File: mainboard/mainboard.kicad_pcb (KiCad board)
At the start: 2 copper layers, 88.9 x 94 mm, 77 parts, among them U1 74HC04, U2 AS6C4008, U3 74HC32, U4 74HC00, U5 SST39SF040, U6 NE555, U7 74HCT245, U8 74HC574, U9 74HC574, Y1 Crystal

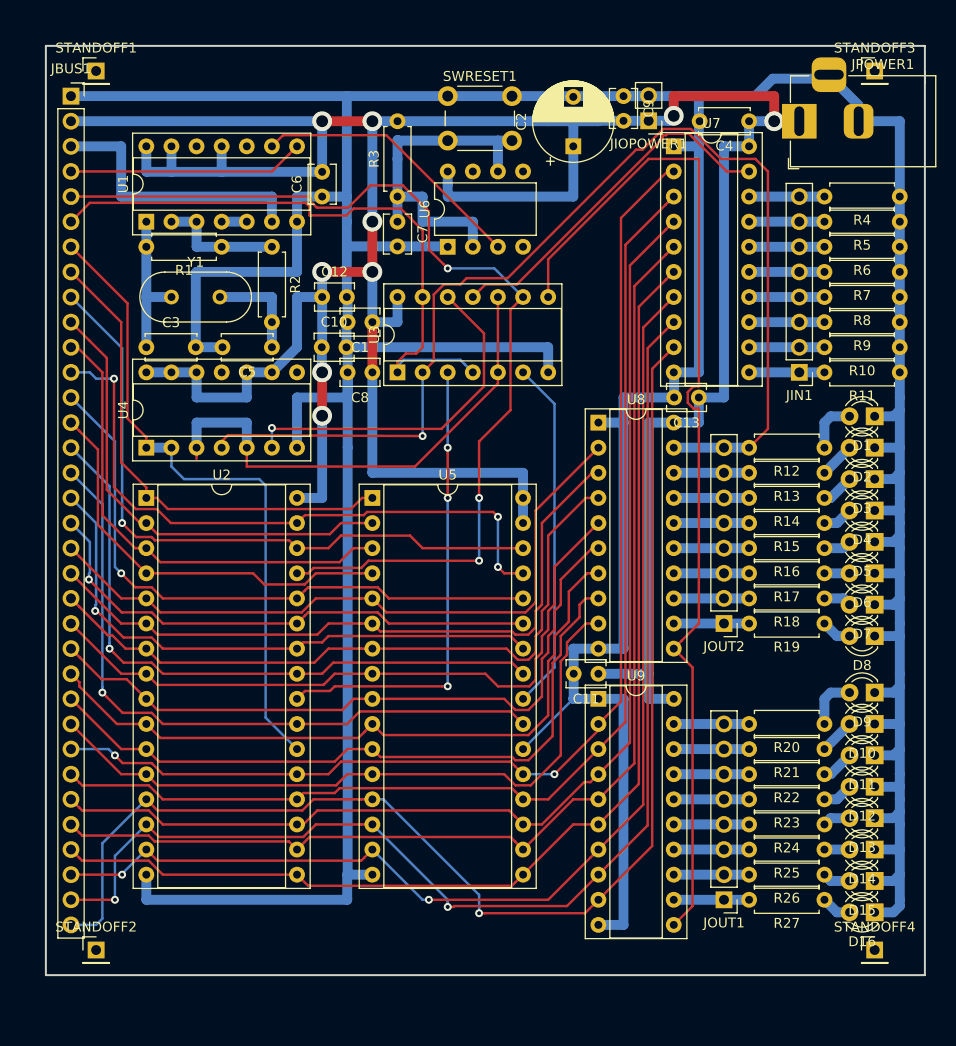
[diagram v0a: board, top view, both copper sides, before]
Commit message: Main board layout tweaks
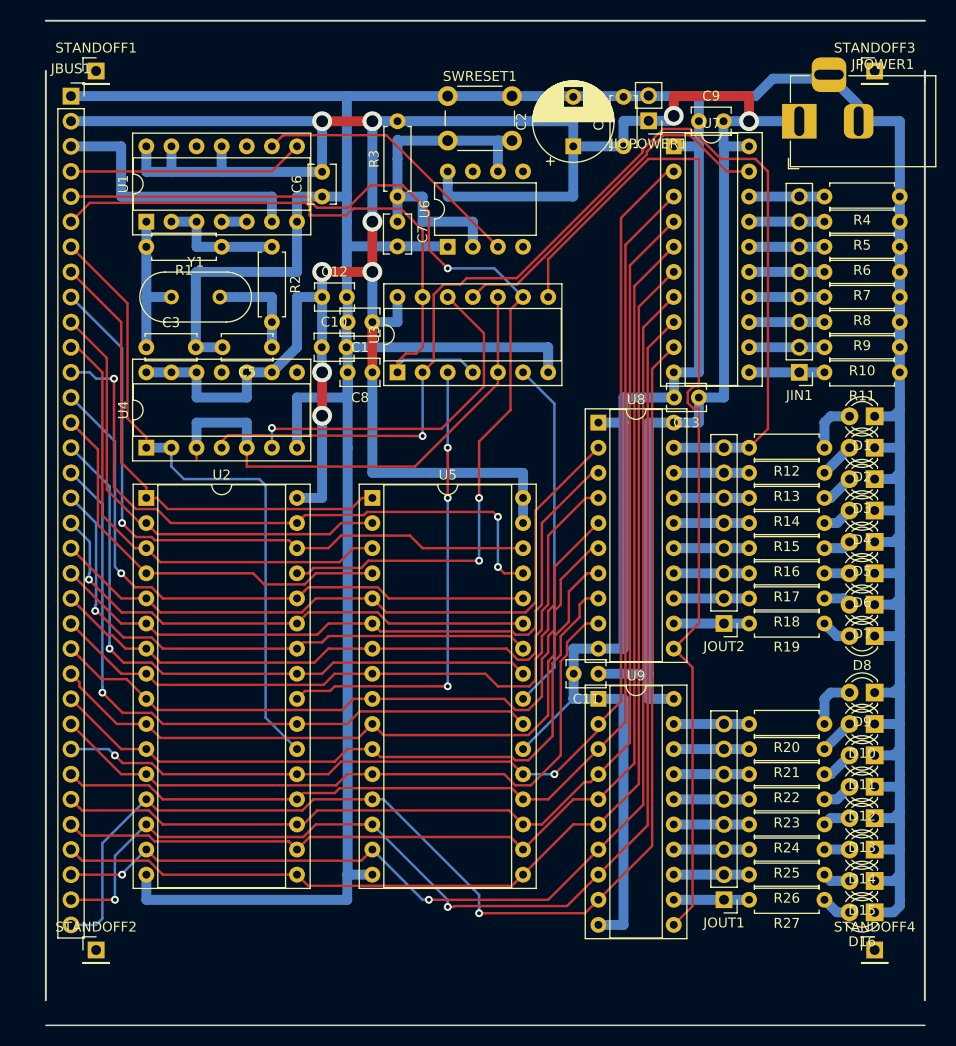
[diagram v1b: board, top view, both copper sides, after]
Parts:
- C3, C5: value 22pF -> 47pF
- moved C4 13.0 mm to (124.5, 50.8), turned to 90 degrees
- moved C9 8.03 mm to (132.1, 48.3), turned to 0 degrees
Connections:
- net Net-(U2-Pad24) renamed /OERAM
- net Net-(U3-Pad11) renamed /RDIN
- net Net-(U3-Pad12) renamed /XX
- net Net-(U3-Pad6) renamed /OEROM
- net Net-(U3-Pad8) renamed /WROUT
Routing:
- net +5V: track 331.2 -> 333.8 mm
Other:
- board size 88.9 x 94 mm -> 88.9 x 101.6 mm

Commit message: More PCB design First tiny program running
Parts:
- removed C12: 100nF, Capacitor_THT:C_Disc_D3.8mm_W2.6mm_P2.50mm
- removed D10, D11, D12, D13, D14, D15, D16, D8, D9: LED_Small, LED_THT:LED_D3.0mm
- removed JOUT2: Conn_01x08_Male, Connector_PinHeader_2.54mm:PinHeader_1x08_P2.54mm_Vertical
- removed R12, R13, R14, R15, R16, R17, R18, R19: 1k, Resistor_THT:R_Axial_DIN0207_L6.3mm_D2.5mm_P7.62mm_Horizontal
- removed STANDOFF1, STANDOFF2, STANDOFF3, STANDOFF4: Conn_01x01_Male, Connector_PinHeader_2.54mm:PinHeader_1x01_P2.54mm_Vertical
- removed U8: 74HC574, Package_DIP:DIP-20_W7.62mm_Socket
- added D0: LED_Small, LED_THT:LED_D3.0mm, F.Cu at (149.9, 124.5)
- added REF**: MountingHole_3.2mm_M3_DIN965_Pad, MountingHole:MountingHole_3.2mm_M3_DIN965_Pad, F.Cu at (73.7, 132.1)
- added REF**: MountingHole_3.2mm_M3_DIN965_Pad, MountingHole:MountingHole_3.2mm_M3_DIN965_Pad, F.Cu at (147.3, 132.1)
- added REF**: MountingHole_3.2mm_M3_DIN965_Pad, MountingHole:MountingHole_3.2mm_M3_DIN965_Pad, F.Cu at (147.3, 53.3)
- added REF**: MountingHole_3.2mm_M3_DIN965_Pad, MountingHole:MountingHole_3.2mm_M3_DIN965_Pad, F.Cu at (73.7, 53.3)
- R10, R11, R4, R5, R6, R7, R8, R9: value 10k -> 22k
- U3: value 74HC32 -> 74AC32
- U4: value 74HC00 -> 74AC00
- U7: value 74HCT245 -> 74HC245
- moved D1 43.2 mm to (149.9, 121.3)
- moved D2 36.8 mm to (149.9, 118.1)
- moved C11 33.9 mm to (129.5, 71.1)
- moved C9 30.7 mm to (116.8, 74.9), turned to 180 degrees
- moved D3 30.5 mm to (149.9, 114.9)
- moved JIOPOWER1 29.0 mm to (134.6, 76.2)
- moved Y1 28.4 mm to (106.7, 71.1), turned to 90 degrees
- moved C6 27.9 mm to (94.0, 83.8), turned to 270 degrees
- moved JIN1 26.5 mm to (134.6, 99.1)
- moved R11 26.5 mm to (144.8, 99.1)
- moved R7 26.5 mm to (144.8, 88.9)
- moved R9 26.5 mm to (144.8, 94.0)
- moved R4 26.5 mm to (144.8, 81.3)
- moved R6 26.5 mm to (144.8, 86.4)
- moved R10 26.5 mm to (144.8, 96.5)
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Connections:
- JOUT1 pad 8: Net-(JOUT1-Pad8) -> /RAM_INHIBIT
- R20 pad 1: Net-(D9-Pad2) -> Net-(D7-Pad2)
- R20 pad 2: Net-(JOUT1-Pad8) -> /RAM_INHIBIT
- R21 pad 1: Net-(D10-Pad2) -> Net-(D6-Pad2)
- R22 pad 1: Net-(D11-Pad2) -> Net-(D5-Pad2)
- R23 pad 1: Net-(D12-Pad2) -> Net-(D4-Pad2)
- R24 pad 1: Net-(D13-Pad2) -> Net-(D3-Pad2)
- R25 pad 1: Net-(D14-Pad2) -> Net-(D2-Pad2)
- R26 pad 1: Net-(D15-Pad2) -> Net-(D1-Pad2)
- U1 pad 4: Net-(U1-Pad4) -> /CLK
- U1 pad 5: Net-(U1-Pad4) -> Net-(U1-Pad5)
- U1 pad 6: /CLK -> /RES
- U1 pad 8: /RES -> Net-(U1-Pad8)
- U1 pad 9: Net-(U1-Pad9) -> +5V
- U6 pad 3: Net-(U1-Pad9) -> Net-(U1-Pad5)
- U9 pad 19: Net-(JOUT1-Pad8) -> /RAM_INHIBIT
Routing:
- net GND: track 513.2 -> 0.00 mm
- net +5V: track 333.8 -> 275.9 mm, vias 9 -> 1
- net /OERAM: track 47.5 -> 91.5 mm, vias 3 -> 0
- net /A2: track 70.2 -> 34.1 mm
- net /A5: track 70.0 -> 34.1 mm
- net /A1: track 69.9 -> 34.0 mm
- net /A0: track 69.9 -> 34.1 mm
- net /A7: track 69.5 -> 34.1 mm
- net /A6: track 69.4 -> 34.1 mm
- net /A3: track 69.4 -> 34.1 mm
- net /A4: track 69.3 -> 34.1 mm
- net Net-(U1-Pad5): track 0.00 -> 32.7 mm
- net /A19N: track 50.8 -> 18.3 mm
- net Net-(U1-Pad9): track 28.0 -> 0.00 mm
- net /OEROM: track 35.7 -> 59.2 mm
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- added copper zone on B.Cu, net GND
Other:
- board size 88.9 x 101.6 mm -> 88.9 x 88.9 mm
- board text added: "5V"
- board text added: "A0"
- board text added: "A1"
- board text added: "A10"
- board text added: "A11"
- board text added: "A12"
- board text added: "A13"
- board text added: "A14"
- board text added: "A15"
- board text added: "A16"
- board text added: "A17"
- board text added: "A18"
- board text added: "A19"
- board text added: "A2"
- board text added: "A3"
- board text added: "A4"
- board text added: "A5"
- board text added: "A6"
- board text added: "A7"
- board text added: "A8"
- board text added: "A9"
- board text added: "Byte Machine - main board Rev. 1 github.com/c0pperdragon/ByteMachine"
- board text added: "CLK"
- board text added: "D0"
- board text added: "D1"
- board text added: "D2"
- board text added: "D3"
- board text added: "D4"
- board text added: "D5"
- board text added: "D6"
- board text added: "D7"
- board text added: "GND"
- board text added: "Power: 5V, 250mA center positive"
- board text added: "RD"
- board text added: "RES"
- board text added: "WR"

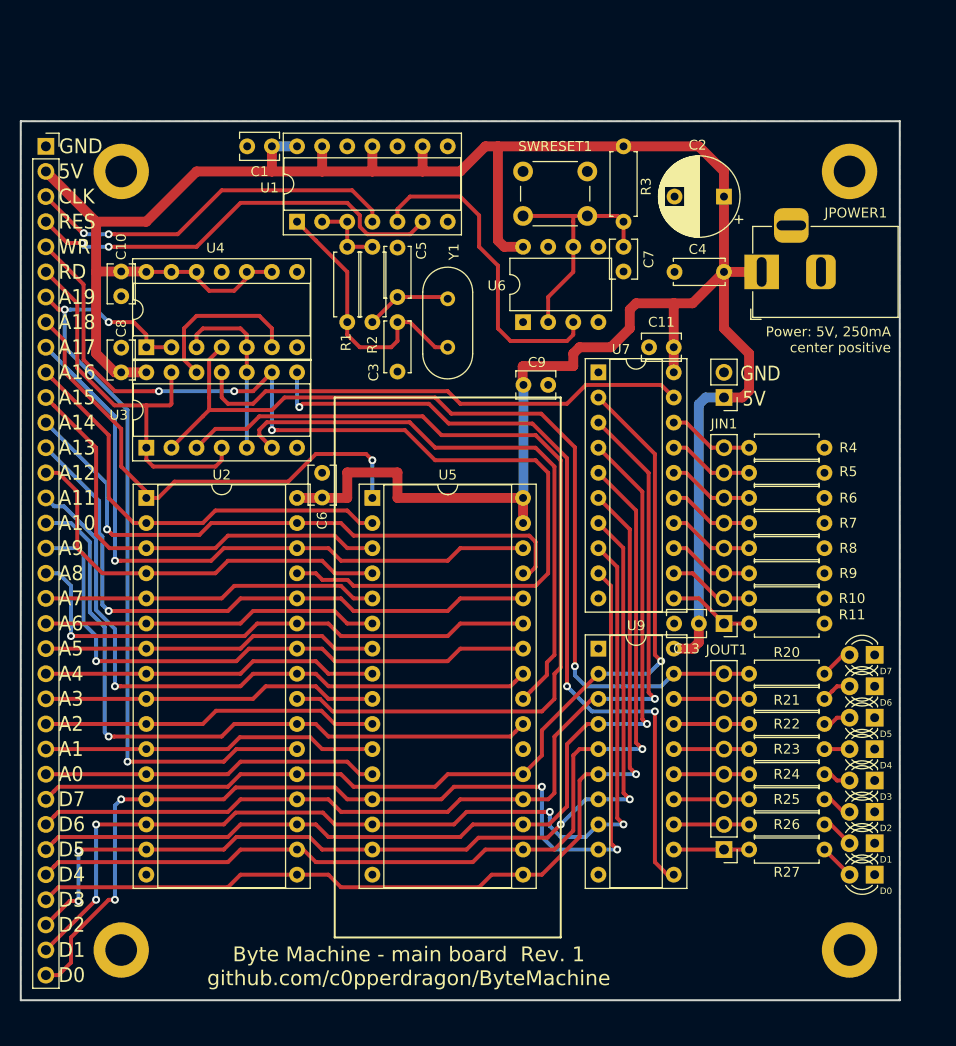
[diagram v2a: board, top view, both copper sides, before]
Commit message: Repurposing this repo (and product name) for my gernic 8-bit computer main board.
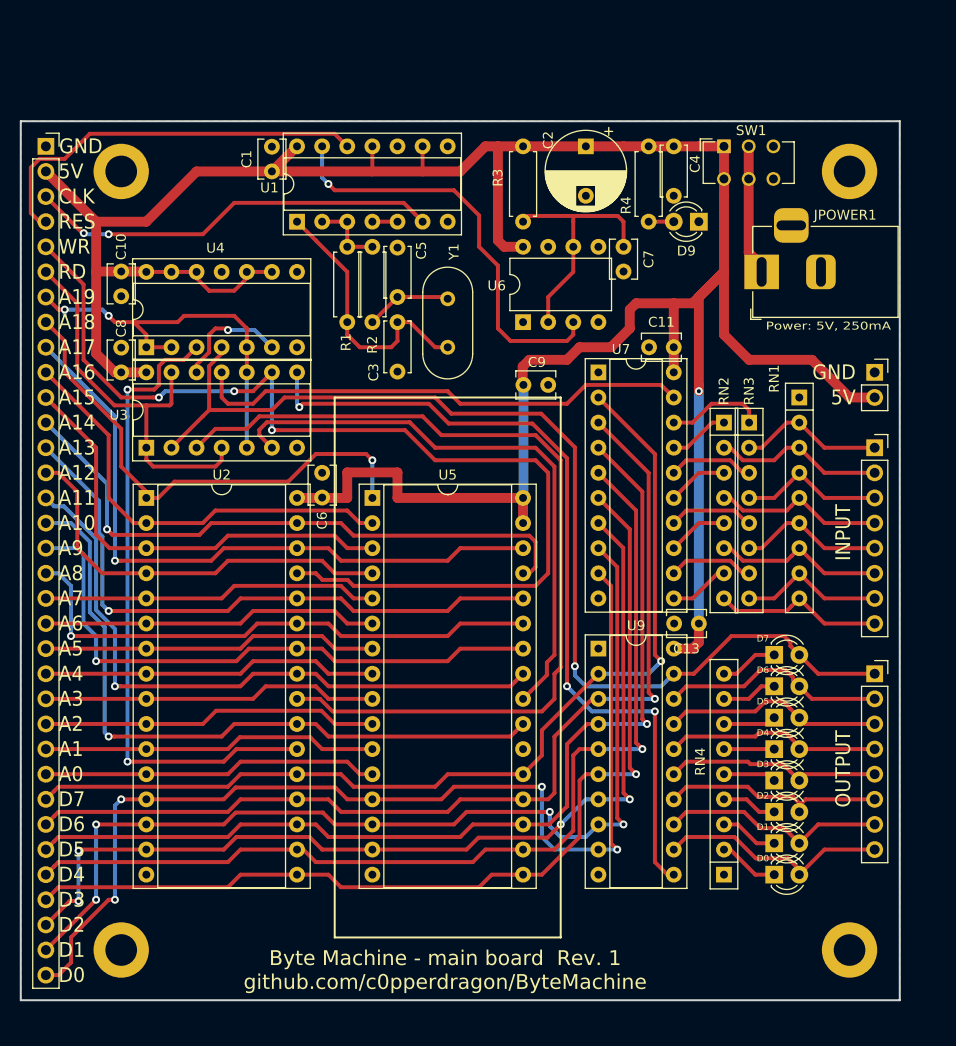
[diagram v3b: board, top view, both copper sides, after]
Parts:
- removed R10, R11, R5, R6, R7, R8, R9: 22k, Resistor_THT:R_Axial_DIN0207_L6.3mm_D2.5mm_P7.62mm_Horizontal
- removed R20, R21, R22, R23, R24, R25, R26, R27: 1k, Resistor_THT:R_Axial_DIN0207_L6.3mm_D2.5mm_P7.62mm_Horizontal
- removed SWRESET1: SW_Push, Button_Switch_THT:SW_PUSH_6mm
- added D9: LED_Small, LED_THT:LED_D3.0mm, F.Cu at (132.1, 58.4)
- added RN1: 22k, Resistor_THT:R_Array_SIP9, F.Cu at (142.2, 76.2)
- added RN2: 1k, Resistor_THT:R_Array_SIP8, F.Cu at (134.6, 78.7)
- added RN3: 1k, Resistor_THT:R_Array_SIP8, F.Cu at (137.2, 78.7)
- added RN4: 1k, Resistor_THT:R_Array_SIP9, F.Cu at (134.6, 124.5)
- added SW1: SW_DPDT_x2, Button_Switch_THT:SW_CuK_JS202011CQN_DPDT_Straight, F.Cu at (134.6, 50.8)
- JIN1, JOUT1: value Conn_01x08_Male -> Conn_01x08_Female; footprint Connector_PinHeader_2.54mm:PinHeader_1x08_P2.54mm_Vertical -> Connector_PinSocket_2.54mm:PinSocket_1x08_P2.54mm_Vertical
- JIOPOWER1: value Conn_01x02_Male -> Conn_01x02_Female; footprint Connector_PinHeader_2.54mm:PinHeader_1x02_P2.54mm_Vertical -> Connector_PinSocket_2.54mm:PinSocket_1x02_P2.54mm_Vertical
- R3: value 470k -> 1M
- R4: value 22k -> 1k
- moved R4 35.3 mm to (127.0, 50.8), turned to 270 degrees
- moved JIN1 23.4 mm to (149.9, 81.3), turned to 0 degrees
- moved JOUT1 23.4 mm to (149.9, 104.1), turned to 0 degrees
- moved JIOPOWER1 15.5 mm to (149.9, 73.7), turned to 0 degrees
- moved C2 14.9 mm to (120.7, 50.8), turned to 270 degrees
- moved C4 13.7 mm to (129.5, 50.8), turned to 270 degrees
- moved D0 10.2 mm to (139.7, 124.5), turned to 0 degrees
- moved D1 10.2 mm to (139.7, 121.3), turned to 0 degrees
- moved D2 10.2 mm to (139.7, 118.1), turned to 0 degrees
- moved D3 10.2 mm to (139.7, 114.9), turned to 0 degrees
- moved D4 10.2 mm to (139.7, 111.8), turned to 0 degrees
- moved D5 10.2 mm to (139.7, 108.6), turned to 0 degrees
- moved D6 10.2 mm to (139.7, 105.4), turned to 0 degrees
- moved D7 10.2 mm to (139.7, 102.2), turned to 0 degrees
- moved R3 10.2 mm to (114.3, 58.4)
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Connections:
- D0 pad 1: GND -> Net-(D0-Pad1)
- D1 pad 1: GND -> Net-(D1-Pad1)
- D2 pad 1: GND -> Net-(D2-Pad1)
- D3 pad 1: GND -> Net-(D3-Pad1)
- D4 pad 1: GND -> Net-(D4-Pad1)
- D5 pad 1: GND -> Net-(D5-Pad1)
- D6 pad 1: GND -> Net-(D6-Pad1)
- D7 pad 1: GND -> Net-(D7-Pad1)
- D7 pad 2: Net-(D7-Pad2) -> /RAM_INHIBIT
- JIOPOWER1 pad 1: +5V -> GND
- JIOPOWER1 pad 2: GND -> +5V
- JOUT1 pad 1: Net-(JOUT1-Pad1) -> /RAM_INHIBIT
- JOUT1 pad 2: Net-(JOUT1-Pad2) -> Net-(D6-Pad2)
- JOUT1 pad 3: Net-(JOUT1-Pad3) -> Net-(D5-Pad2)
- JOUT1 pad 4: Net-(JOUT1-Pad4) -> Net-(D4-Pad2)
- JOUT1 pad 5: Net-(JOUT1-Pad5) -> Net-(D3-Pad2)
- JOUT1 pad 6: Net-(JOUT1-Pad6) -> Net-(D2-Pad2)
- JOUT1 pad 7: Net-(JOUT1-Pad7) -> Net-(D1-Pad2)
- JOUT1 pad 8: /RAM_INHIBIT -> Net-(D0-Pad2)
- JPOWER1 pad 1: +5V -> Net-(JPOWER1-Pad1)
- R4 pad 1: GND -> +5V
- R4 pad 2: Net-(JIN1-Pad8) -> Net-(D9-Pad2)
- U1 pad 12: Net-(U1-Pad12) -> /RES
- U1 pad 13: +5V -> Net-(U1-Pad13)
- U1 pad 4: /CLK -> Net-(U1-Pad4)
- U1 pad 5: Net-(U1-Pad5) -> Net-(U1-Pad4)
- U1 pad 6: /RES -> /CLK
- U2 pad 22: /A19 -> /CERAM
- U3 pad 10: /A19N -> /A19
- U3 pad 5: /A19N -> /A19
- U4 pad 3: /A19N -> /CERAM
- U4 pad 5: /A19N -> /A19
- U6 pad 3: Net-(U1-Pad5) -> Net-(U1-Pad13)
- U7 pad 11: Net-(JIN1-Pad1) -> Net-(RN2-Pad7)
- U7 pad 12: Net-(JIN1-Pad2) -> Net-(RN3-Pad7)
- U7 pad 13: Net-(JIN1-Pad3) -> Net-(RN2-Pad5)
- U7 pad 14: Net-(JIN1-Pad4) -> Net-(RN3-Pad5)
- U7 pad 15: Net-(JIN1-Pad5) -> Net-(RN2-Pad3)
- U7 pad 16: Net-(JIN1-Pad6) -> Net-(RN3-Pad3)
- U7 pad 17: Net-(JIN1-Pad7) -> Net-(RN2-Pad1)
- U7 pad 18: Net-(JIN1-Pad8) -> Net-(RN3-Pad1)
- U9 pad 12: Net-(JOUT1-Pad1) -> Net-(D0-Pad2)
- U9 pad 13: Net-(JOUT1-Pad2) -> Net-(D1-Pad2)
- U9 pad 14: Net-(JOUT1-Pad3) -> Net-(D2-Pad2)
- U9 pad 15: Net-(JOUT1-Pad4) -> Net-(D3-Pad2)
- U9 pad 16: Net-(JOUT1-Pad5) -> Net-(D4-Pad2)
- U9 pad 17: Net-(JOUT1-Pad6) -> Net-(D5-Pad2)
- U9 pad 18: Net-(JOUT1-Pad7) -> Net-(D6-Pad2)
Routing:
- net /CERAM: track 0.00 -> 65.2 mm, vias 0 -> 2
- net Net-(U1-Pad13): track 0.00 -> 42.5 mm, vias 0 -> 1
- net /A19: track 81.6 -> 40.4 mm, vias 3 -> 2
- net Net-(U1-Pad5): track 32.7 -> 0.00 mm
- net Net-(D0-Pad2): track 3.59 -> 23.8 mm
- net Net-(D6-Pad2): track 3.07 -> 22.9 mm
- net Net-(D1-Pad2): track 3.33 -> 23.0 mm
- net Net-(D2-Pad2): track 3.07 -> 22.7 mm
- net Net-(D3-Pad2): track 2.80 -> 22.3 mm
- net Net-(D5-Pad2): track 2.80 -> 22.2 mm
- net Net-(D4-Pad2): track 2.54 -> 21.9 mm
- net /A19N: track 18.3 -> 0.00 mm
- net /RAM_INHIBIT: track 93.5 -> 109.6 mm
- net +5V: track 275.9 -> 289.5 mm
- net Net-(JPOWER1-Pad1): track 0.00 -> 13.2 mm
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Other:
- board text added: "INPUT"
- board text added: "OUTPUT"
- board text added: "Power: 5V, 250mA"
- board text removed: "Power: 5V, 250mA center positive"

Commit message: Redesign port access to use a state flip-flop made of NANDs instead of wasting a bit of the dedicatd output IC.
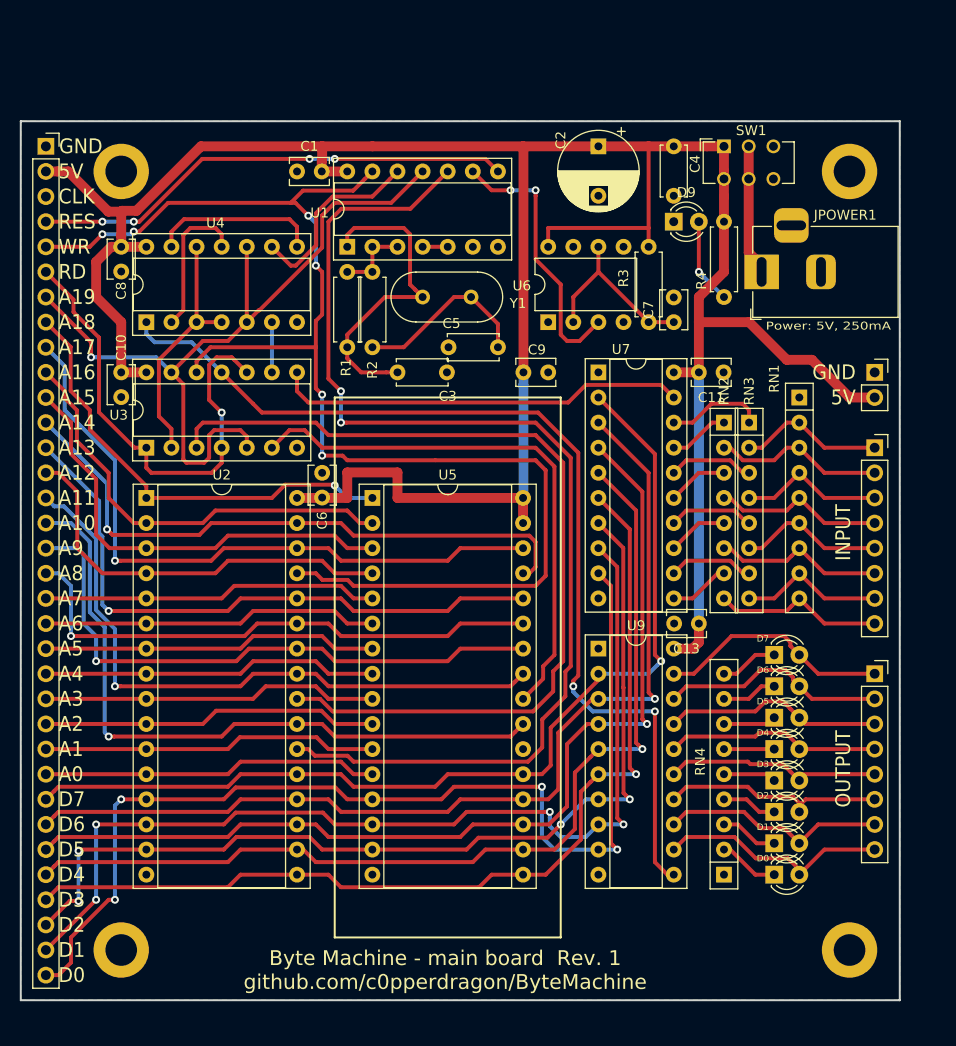
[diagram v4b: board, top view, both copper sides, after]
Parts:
- C3, C5: value 47pF -> 33pF
- U1: value 74HC04 -> 74AC04
- moved R3 16.3 mm to (127.0, 68.6)
- moved C8 12.7 mm to (73.7, 61.0), turned to 270 degrees
- moved C5 11.4 mm to (111.8, 71.1), turned to 180 degrees
- moved R4 10.8 mm to (134.6, 58.4)
- moved C10 10.2 mm to (73.7, 73.7)
- moved C7 9.16 mm to (129.5, 68.6), turned to 90 degrees
- moved Y1 5.68 mm to (104.1, 66.0), turned to 0 degrees
- moved U1 5.68 mm to (96.5, 61.0)
- moved C3 5.08 mm to (101.6, 73.7), turned to 0 degrees
- moved C11 3.59 mm to (132.1, 73.7), turned to 0 degrees
- moved D9 2.54 mm to (129.5, 58.4), turned to 0 degrees
- moved U4 2.54 mm to (76.2, 68.6)
- moved U6 2.54 mm to (116.8, 68.6)
- moved R1 2.54 mm to (96.5, 63.5)
- moved R2 2.54 mm to (99.1, 63.5)
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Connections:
- C1 pad 1: +5V -> GND
- C1 pad 2: GND -> +5V
- D7 pad 2: /RAM_INHIBIT -> Net-(D7-Pad2)
- JOUT1 pad 1: /RAM_INHIBIT -> Net-(D7-Pad2)
- U1 pad 10: Net-(U1-Pad10) -> /CERAM
- U1 pad 11: +5V -> /A19
- U1 pad 12: /RES -> Net-(U1-Pad12)
- U1 pad 13: Net-(U1-Pad13) -> /WR
- U1 pad 8: Net-(U1-Pad8) -> /RES
- U1 pad 9: +5V -> Net-(U1-Pad9)
- U3 pad 10: /A19 -> /RD
- U3 pad 11: /RDIN -> /CPOUTPUT
- U3 pad 12: /XX -> /WR
- U3 pad 13: /RD -> /A19
- U3 pad 2: /RAM_INHIBIT -> /IOMODE
- U3 pad 8: /WROUT -> /OEINPUT
- U3 pad 9: /WR -> Net-(U3-Pad9)
- U4 pad 1: /A19 -> /CPOUTPUT
- U4 pad 10: +5V -> /A19
- U4 pad 12: +5V -> /IOMODE
- U4 pad 13: +5V -> /RESETIO
- U4 pad 2: /A19 -> Net-(U4-Pad11)
- U4 pad 3: /CERAM -> /IOMODE
- U4 pad 4: /RAM_INHIBIT -> /IOMODE
- U4 pad 6: /XX -> Net-(U3-Pad9)
- U4 pad 8: Net-(U4-Pad8) -> /RESETIO
- U4 pad 9: +5V -> Net-(U1-Pad12)
- U6 pad 3: Net-(U1-Pad13) -> Net-(U1-Pad9)
- U7 pad 19: /RDIN -> /OEINPUT
- U9 pad 11: /WROUT -> /CPOUTPUT
- U9 pad 19: /RAM_INHIBIT -> Net-(D7-Pad2)
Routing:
- net /RAM_INHIBIT: track 109.6 -> 0.00 mm, vias 1 -> 0
- net /CPOUTPUT: track 0.00 -> 101.0 mm, vias 0 -> 2
- net /WROUT: track 83.8 -> 0.00 mm, vias 3 -> 0
- net /CERAM: track 65.2 -> 116.1 mm
- net /RDIN: track 50.9 -> 0.00 mm
- net Net-(U1-Pad13): track 42.5 -> 0.00 mm, vias 1 -> 0
- net /CLK: track 41.8 -> 0.00 mm, vias 2 -> 0
- net /OEINPUT: track 0.00 -> 41.7 mm
- net /A19: track 40.4 -> 80.1 mm, vias 2 -> 1
- net /WR: track 106.9 -> 137.6 mm, vias 3 -> 6
- net Net-(U1-Pad9): track 0.00 -> 27.7 mm, vias 0 -> 2
- net /IOMODE: track 0.00 -> 25.0 mm
- net Net-(D7-Pad2): track 0.00 -> 23.7 mm
- net +5V: track 289.5 -> 268.9 mm, vias 1 -> 0
- net Net-(U1-Pad12): track 0.00 -> 19.3 mm
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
